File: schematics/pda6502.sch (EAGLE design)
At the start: 11 parts, among them IC1 DS1813-SMD, U1 W65C02S, U2 W65C22S, U3 KM28C64A-25, U4 UM61256AK-12

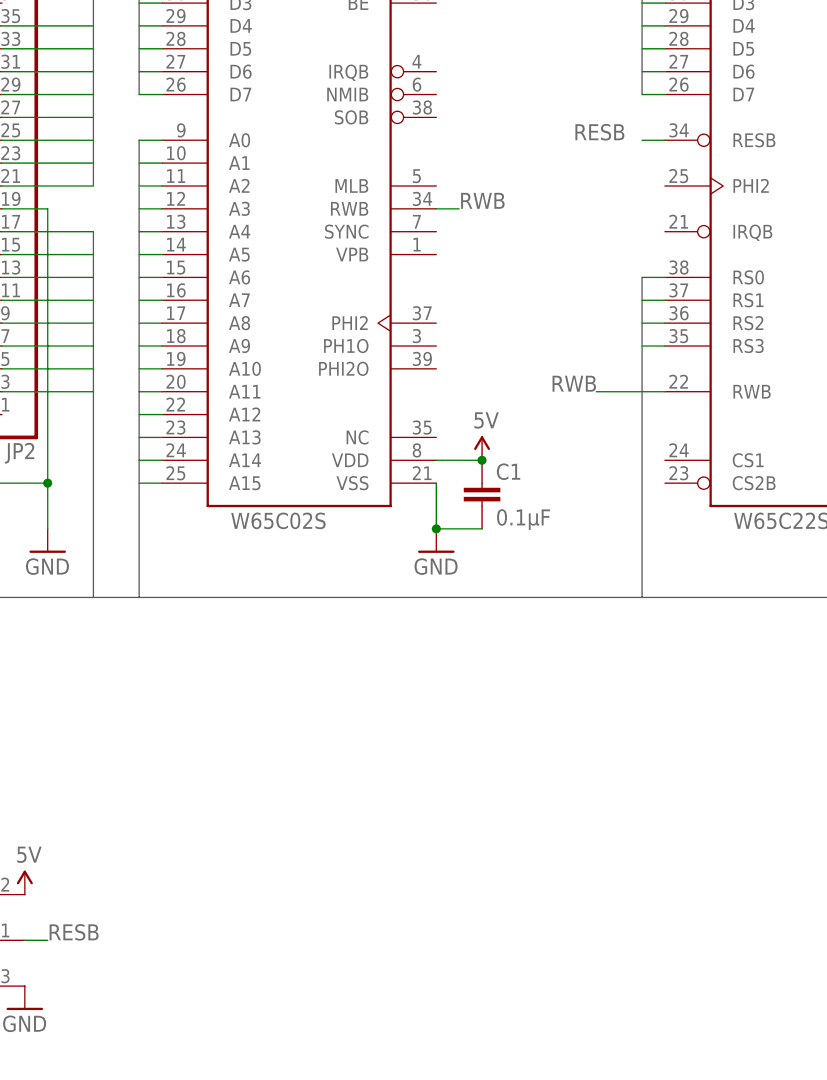
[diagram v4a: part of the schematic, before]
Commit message: schematics: crystal oscillator; half can.
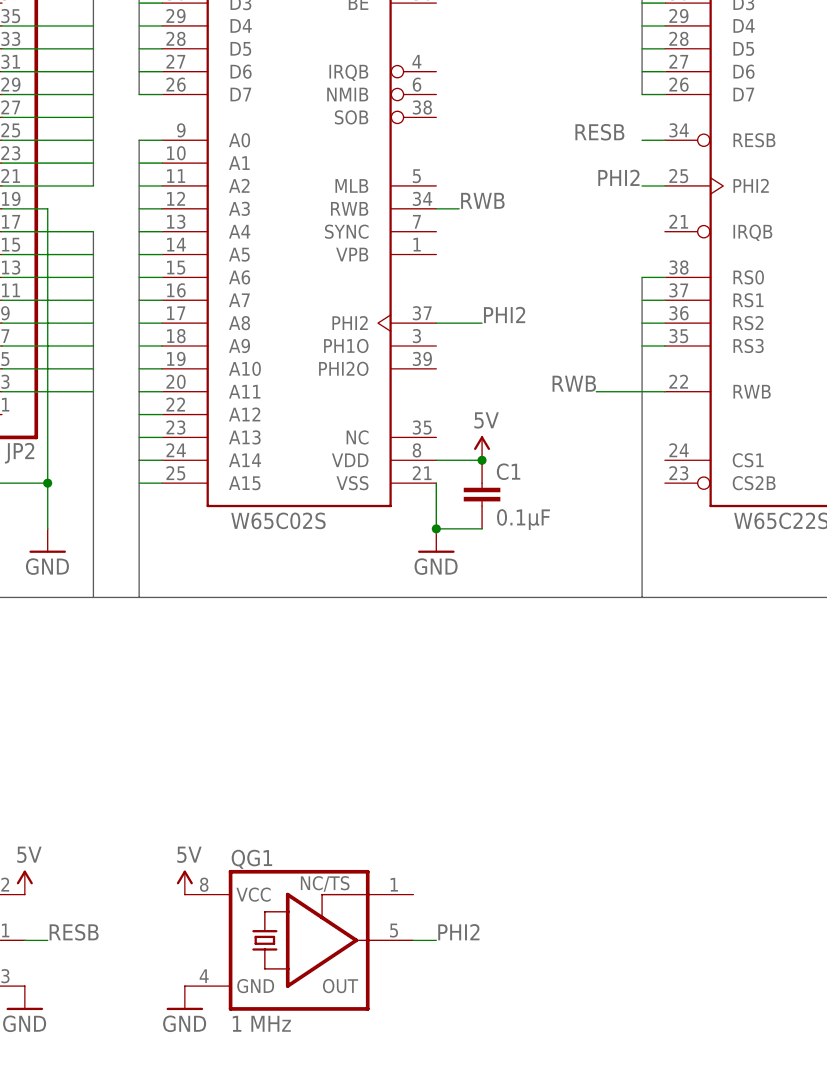
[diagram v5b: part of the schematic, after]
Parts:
- added QG1: 1 MHz, crystal:XO-8
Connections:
- new net PHI2: QG1.OUT, U2.PHI2
- net 5V: now also QG1.VCC
- net GND: now also QG1.GND
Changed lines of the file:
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@@
 <part name="SUPPLY6" library="SparkFun-Aesthetics" deviceset="5V" device=""/>
 <part name="GND5" library="SparkFun-Aesthetics" deviceset="GND" device=""/>
+<part name="QG1" library="crystal" deviceset="XO-" device="8" value="1 MHz"/>
+<part name="SUPPLY7" library="SparkFun-Aesthetics" deviceset="5V" device=""/>
+<part name="GND8" library="SparkFun-Aesthetics" deviceset="GND" device=""/>
 </parts>
 <sheets>
@@
 <instance part="SUPPLY6" gate="G$1" x="30.48" y="48.26"/>
 <instance part="GND5" gate="1" x="30.48" y="35.56"/>
+<instance part="QG1" gate="G$1" x="60.96" y="43.18"/>
+<instance part="SUPPLY7" gate="G$1" x="48.26" y="48.26"/>
+<instance part="GND8" gate="1" x="48.26" y="35.56"/>
 </instances>
 <busses>
@@
 <pinref part="GND5" gate="1" pin="GND"/>
 </segment>
+<segment>
+<pinref part="QG1" gate="G$1" pin="GND"/>
+<pinref part="GND8" gate="1" pin="GND"/>
+</segment>
 </net>
 <net name="5V" class="0">
@@
 <pinref part="SUPPLY6" gate="G$1" pin="5V"/>
 </segment>
+<segment>
+<pinref part="QG1" gate="G$1" pin="VCC"/>
+<pinref part="SUPPLY7" gate="G$1" pin="5V"/>
+</segment>
 </net>
 <net name="PA0" class="0">
@@
 </segment>
 </net>
+<net name="PHI2" class="0">
+<segment>
+<pinref part="QG1" gate="G$1" pin="OUT"/>
+<wire x1="73.66" y1="43.18" x2="76.2" y2="43.18" width="0.1524" layer="91"/>
+<label x="76.2" y="43.18" size="1.778" layer="95"/>
+</segment>
+<segment>
+<wire x1="76.2" y1="111.76" x2="81.28" y2="111.76" width="0.1524" layer="91"/>
+<label x="81.28" y="111.76" size="1.778" layer="95"/>
+</segment>
+<segment>
+<pinref part="U2" gate="G$1" pin="PHI2"/>
+<wire x1="101.6" y1="127" x2="99.06" y2="127" width="0.1524" layer="91"/>
+<label x="93.98" y="127" size="1.778" layer="95"/>
+</segment>
+</net>

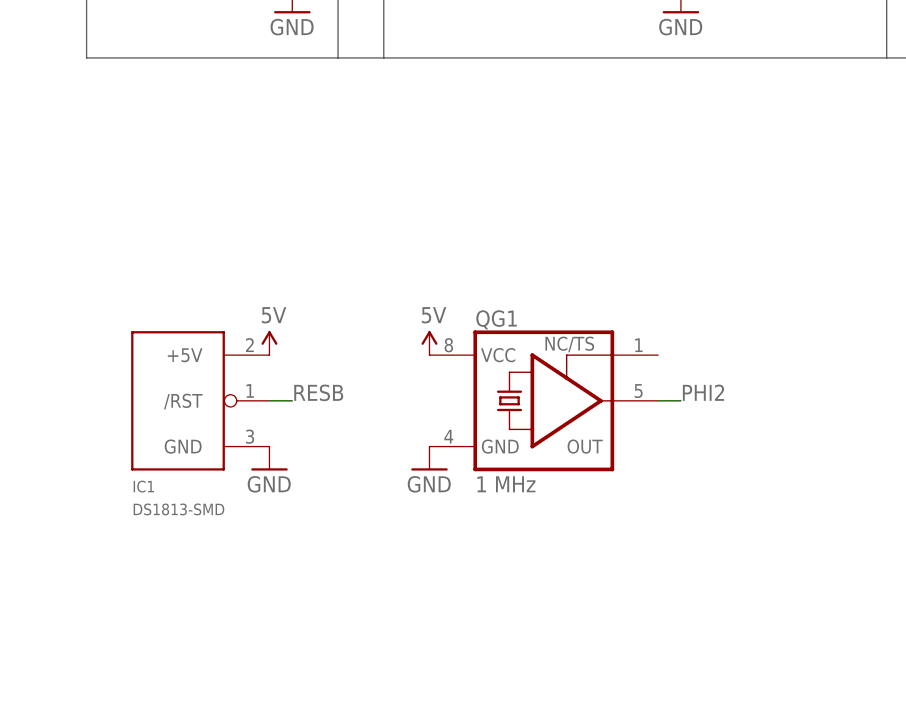
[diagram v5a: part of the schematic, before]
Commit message: schematics: reset circuit has button.
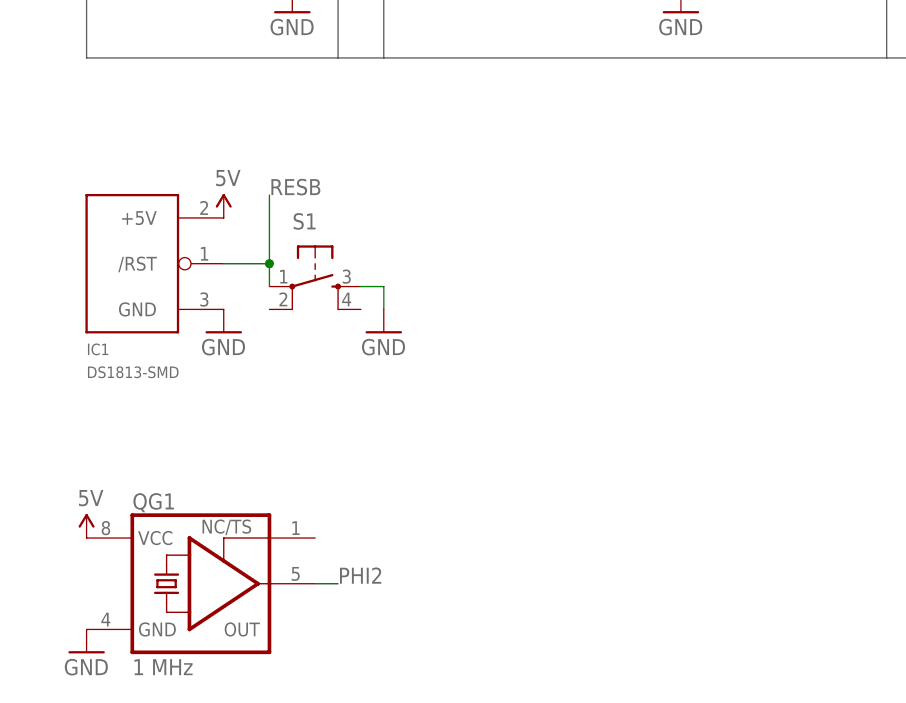
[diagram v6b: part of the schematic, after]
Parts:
- added S1: (no value), SparkFun-Electromechanical:TAC_SWITCHSMD
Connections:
- net GND: now also S1.3
- net RESB: now also S1.1
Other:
- moved on the sheet: IC1, QG1
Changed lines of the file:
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@@
 <part name="SUPPLY7" library="SparkFun-Aesthetics" deviceset="5V" device=""/>
 <part name="GND8" library="SparkFun-Aesthetics" deviceset="GND" device=""/>
+<part name="S1" library="SparkFun-Electromechanical" deviceset="TAC_SWITCH" device="SMD"/>
+<part name="GND9" library="SparkFun-Aesthetics" deviceset="GND" device=""/>
 </parts>
 <sheets>
@@
 <instance part="C3" gate="G$1" x="213.36" y="114.3"/>
 <instance part="C4" gate="G$1" x="261.62" y="96.52"/>
-<instance part="IC1" gate="G$1" x="17.78" y="43.18"/>
-<instance part="SUPPLY6" gate="G$1" x="30.48" y="48.26"/>
-<instance part="GND5" gate="1" x="30.48" y="35.56"/>
-<instance part="QG1" gate="G$1" x="60.96" y="43.18"/>
-<instance part="SUPPLY7" gate="G$1" x="48.26" y="48.26"/>
-<instance part="GND8" gate="1" x="48.26" y="35.56"/>
+<instance part="IC1" gate="G$1" x="12.7" y="58.42"/>
+<instance part="SUPPLY6" gate="G$1" x="25.4" y="63.5"/>
+<instance part="GND5" gate="1" x="25.4" y="50.8"/>
+<instance part="QG1" gate="G$1" x="22.86" y="22.86"/>
+<instance part="SUPPLY7" gate="G$1" x="10.16" y="27.94"/>
+<instance part="GND8" gate="1" x="10.16" y="15.24"/>
+<instance part="S1" gate="S" x="35.56" y="55.88"/>
+<instance part="GND9" gate="1" x="43.18" y="50.8"/>
 </instances>
 <busses>
@@
 <pinref part="GND8" gate="1" pin="GND"/>
 </segment>
+<segment>
+<pinref part="S1" gate="S" pin="3"/>
+<pinref part="GND9" gate="1" pin="GND"/>
+<wire x1="40.64" y1="55.88" x2="43.18" y2="55.88" width="0.1524" layer="91"/>
+<wire x1="43.18" y1="55.88" x2="43.18" y2="53.34" width="0.1524" layer="91"/>
+</segment>
 </net>
 <net name="5V" class="0">
@@
 <net name="RESB" class="0">
 <segment>
-<pinref part="IC1" gate="G$1" pin="/RST"/>
-<wire x1="30.48" y1="43.18" x2="33.02" y2="43.18" width="0.1524" layer="91"/>
-<label x="33.02" y="43.18" size="1.778" layer="95"/>
-</segment>
-<segment>
 <pinref part="U1" gate="G$1" pin="RESB"/>
 <wire x1="76.2" y1="154.94" x2="78.74" y2="154.94" width="0.1524" layer="91"/>
@@
 <label x="91.44" y="132.08" size="1.778" layer="95"/>
 </segment>
+<segment>
+<pinref part="IC1" gate="G$1" pin="/RST"/>
+<wire x1="25.4" y1="58.42" x2="30.48" y2="58.42" width="0.1524" layer="91"/>
+<wire x1="30.48" y1="58.42" x2="30.48" y2="66.04" width="0.1524" layer="91"/>
+<wire x1="30.48" y1="58.42" x2="30.48" y2="55.88" width="0.1524" layer="91"/>
+<junction x="30.48" y="58.42"/>
+<pinref part="S1" gate="S" pin="1"/>
+<label x="30.48" y="66.04" size="1.778" layer="95"/>
+</segment>
 </net>
 <net name="PHI2" class="0">
 <segment>
 <pinref part="QG1" gate="G$1" pin="OUT"/>
-<wire x1="73.66" y1="43.18" x2="76.2" y2="43.18" width="0.1524" layer="91"/>
-<label x="76.2" y="43.18" size="1.778" layer="95"/>
-</segment>
-<segment>
+<wire x1="35.56" y1="22.86" x2="38.1" y2="22.86" width="0.1524" layer="91"/>
+<label x="38.1" y="22.86" size="1.778" layer="95"/>
+</segment>
+<segment>

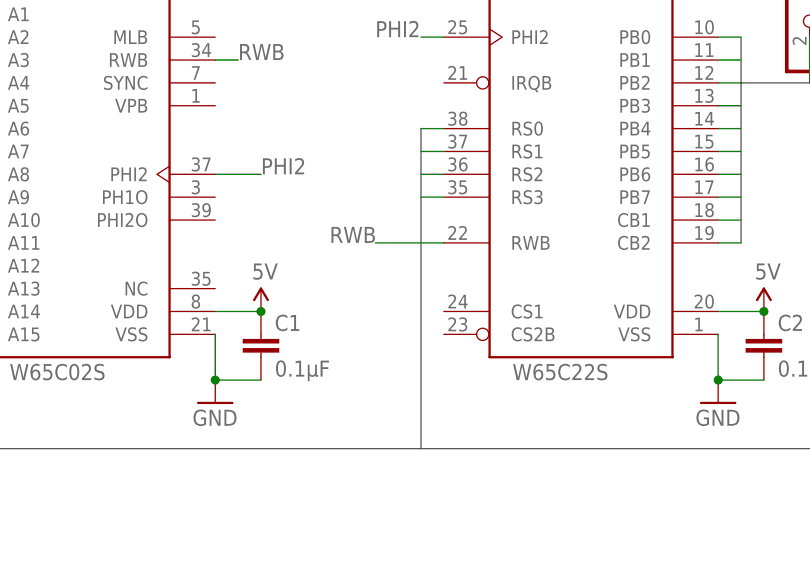
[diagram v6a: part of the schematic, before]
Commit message: schematics: VIA CS1 tied high (active). See active-low CS2B.
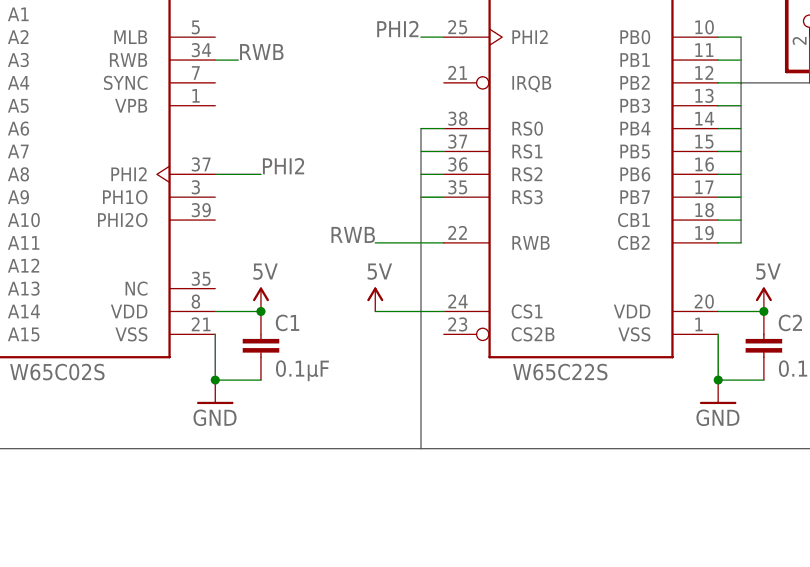
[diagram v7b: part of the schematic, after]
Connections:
- net 5V: now also U2.CS1
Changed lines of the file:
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@@
 <part name="S1" library="SparkFun-Electromechanical" deviceset="TAC_SWITCH" device="SMD"/>
 <part name="GND9" library="SparkFun-Aesthetics" deviceset="GND" device=""/>
+<part name="SUPPLY8" library="SparkFun-Aesthetics" deviceset="5V" device=""/>
 </parts>
 <sheets>
@@
 <instance part="S1" gate="S" x="35.56" y="55.88"/>
 <instance part="GND9" gate="1" x="43.18" y="50.8"/>
+<instance part="SUPPLY8" gate="G$1" x="93.98" y="96.52"/>
 </instances>
 <busses>
@@
 <pinref part="SUPPLY7" gate="G$1" pin="5V"/>
 </segment>
-</net>
+<segment>
+<pinref part="U2" gate="G$1" pin="CS1"/>
+<pinref part="SUPPLY8" gate="G$1" pin="5V"/>
+<wire x1="101.6" y1="96.52" x2="93.98" y2="96.52" width="0.1524" layer="91"/>
+</segment>
+</net>

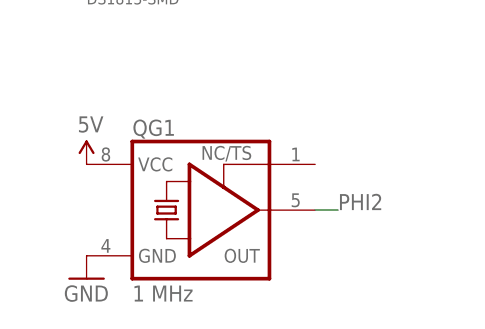
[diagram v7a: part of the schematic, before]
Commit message: schematics: PHI2 net into 6502 fixed; was not connected.
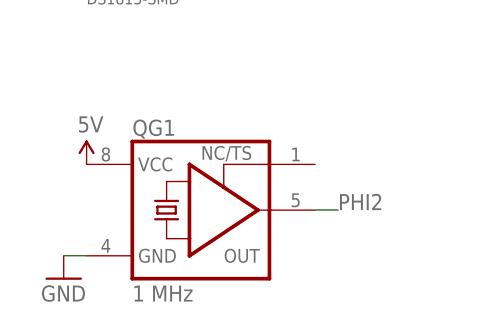
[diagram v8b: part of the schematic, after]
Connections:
- net PHI2: now also U1.PHI2
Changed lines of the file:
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@@
 <instance part="QG1" gate="G$1" x="22.86" y="22.86"/>
 <instance part="SUPPLY7" gate="G$1" x="10.16" y="27.94"/>
-<instance part="GND8" gate="1" x="10.16" y="15.24"/>
+<instance part="GND8" gate="1" x="7.62" y="15.24"/>
 <instance part="S1" gate="S" x="35.56" y="55.88"/>
 <instance part="GND9" gate="1" x="43.18" y="50.8"/>
@@
 </segment>
 <segment>
-<pinref part="QG1" gate="G$1" pin="GND"/>
-<pinref part="GND8" gate="1" pin="GND"/>
-</segment>
-<segment>
 <pinref part="S1" gate="S" pin="3"/>
 <pinref part="GND9" gate="1" pin="GND"/>
 <wire x1="40.64" y1="55.88" x2="43.18" y2="55.88" width="0.1524" layer="91"/>
 <wire x1="43.18" y1="55.88" x2="43.18" y2="53.34" width="0.1524" layer="91"/>
+</segment>
+<segment>
+<pinref part="QG1" gate="G$1" pin="GND"/>
+<pinref part="GND8" gate="1" pin="GND"/>
+<wire x1="10.16" y1="17.78" x2="7.62" y2="17.78" width="0.1524" layer="91"/>
 </segment>
 </net>
@@
 </segment>
 <segment>
-<wire x1="76.2" y1="111.76" x2="81.28" y2="111.76" width="0.1524" layer="91"/>
-<label x="81.28" y="111.76" size="1.778" layer="95"/>
-</segment>
-<segment>
 <pinref part="U2" gate="G$1" pin="PHI2"/>
 <wire x1="101.6" y1="127" x2="99.06" y2="127" width="0.1524" layer="91"/>
 <label x="93.98" y="127" size="1.778" layer="95"/>
 </segment>
-</net>
+<segment>
+<pinref part="U1" gate="G$1" pin="PHI2"/>
+<wire x1="76.2" y1="111.76" x2="81.28" y2="111.76" width="0.1524" layer="91"/>
+<label x="81.28" y="111.76" size="1.778" layer="95"/>
+</segment>
+</net>
